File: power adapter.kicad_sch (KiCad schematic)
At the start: 12 parts

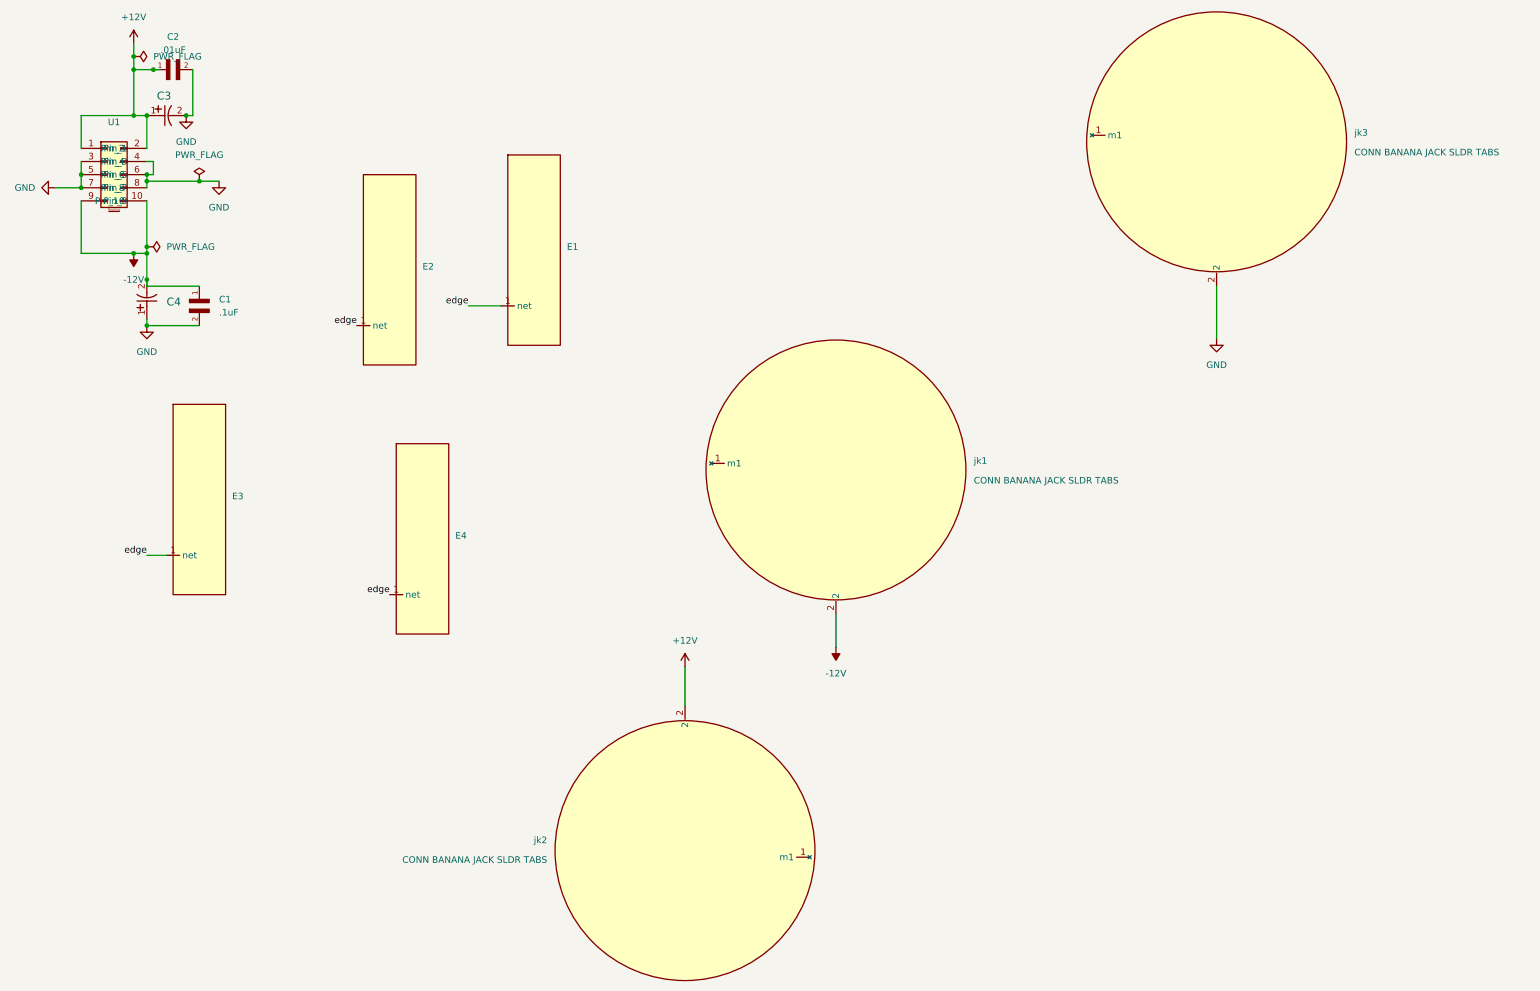
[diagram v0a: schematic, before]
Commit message: added default widths
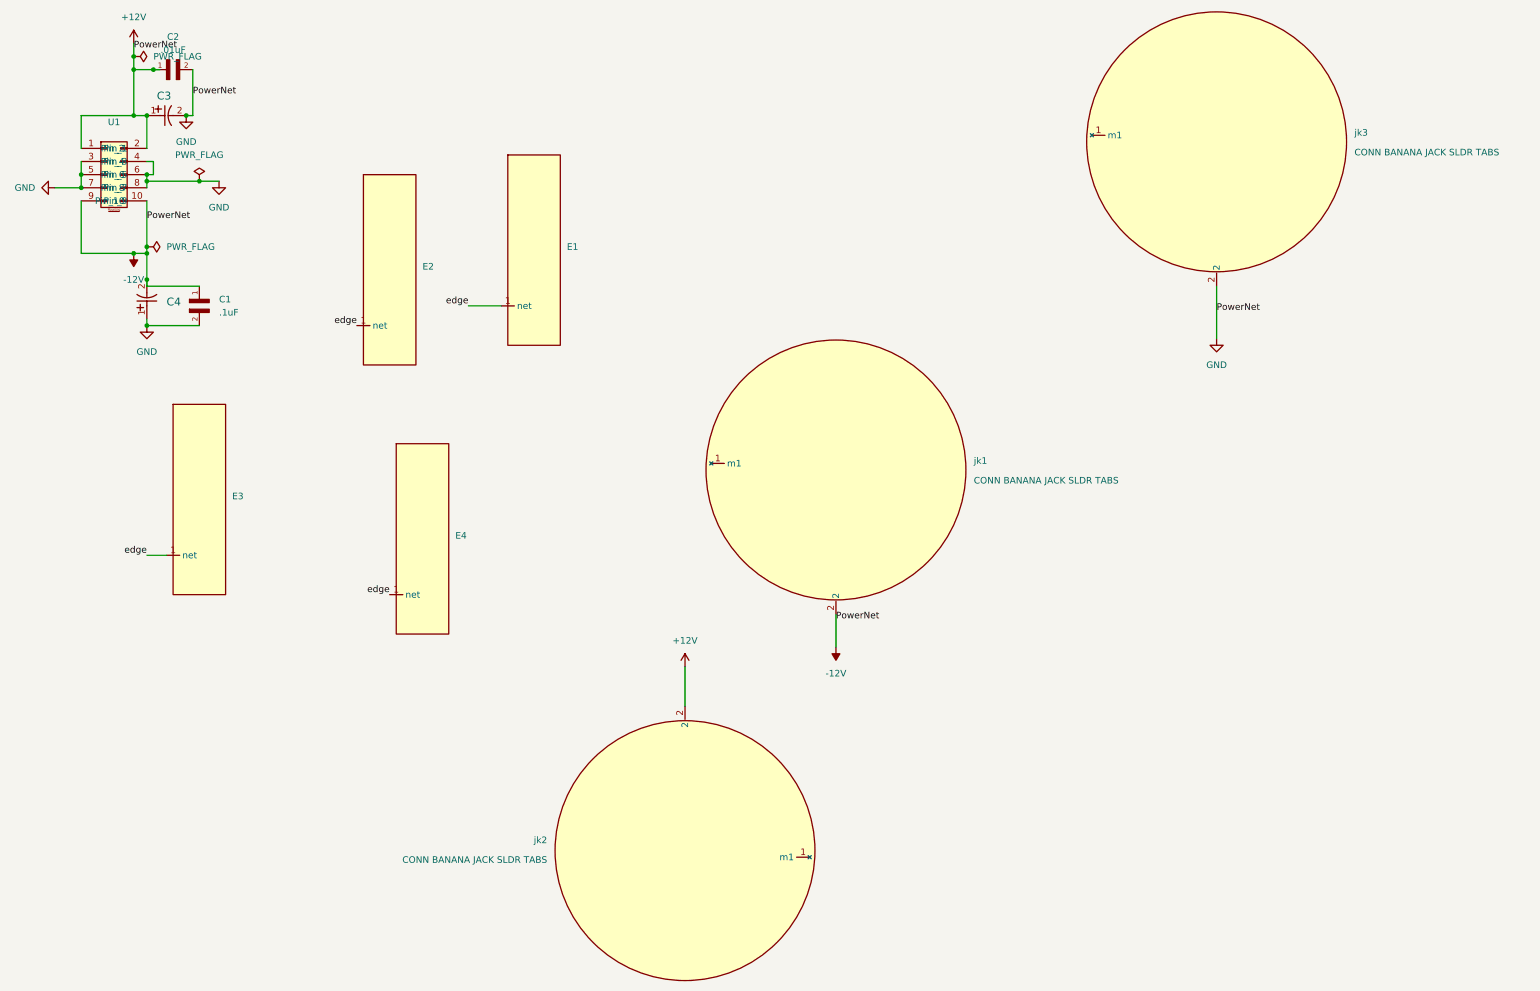
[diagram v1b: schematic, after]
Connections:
- net -12V is gone; now on net +12V: C1.1, C4.2, U1.10 (Pin_10), U1.9 (Pin_9), jk1.2
- net GND is gone; now on net +12V: C1.2, C2.2, C3.2, C4.1, U1.3 (Pin_3), U1.4 (Pin_4), U1.5 (Pin_5), U1.6 (Pin_6), U1.7 (Pin_7), U1.8 (Pin_8), jk3.2
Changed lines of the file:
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@@
+		)
+	)
+	(label "PowerNet"
+		(at 167.64 134.62 0)
+		(effects
+			(font
+				(size 1.27 1.27)
+			)
+			(justify left bottom)
+		)
+	)
+	(label "PowerNet"
+		(at 34.29 57.15 0)
+		(effects
+			(font
+				(size 1.27 1.27)
+			)
+			(justify left bottom)
+		)
+	)
+	(label "PowerNet"
+		(at 31.75 24.13 0)
+		(effects
+			(font
+				(size 1.27 1.27)
+			)
+			(justify left bottom)
 		)
 	)
@@
 			)
 			(justify right bottom)
+		)
+	)
+	(label "PowerNet"
+		(at 43.18 33.02 0)
+		(effects
+			(font
+				(size 1.27 1.27)
+			)
+			(justify left bottom)
 		)
 	)
@@
 		)
 	)
+	(label "PowerNet"
+		(at 241.3 74.93 0)
+		(effects
+			(font
+				(size 1.27 1.27)
+			)
+			(justify left bottom)
+		)
+	)

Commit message: Mk2firstCommit
more attention paid to fixing ERCs
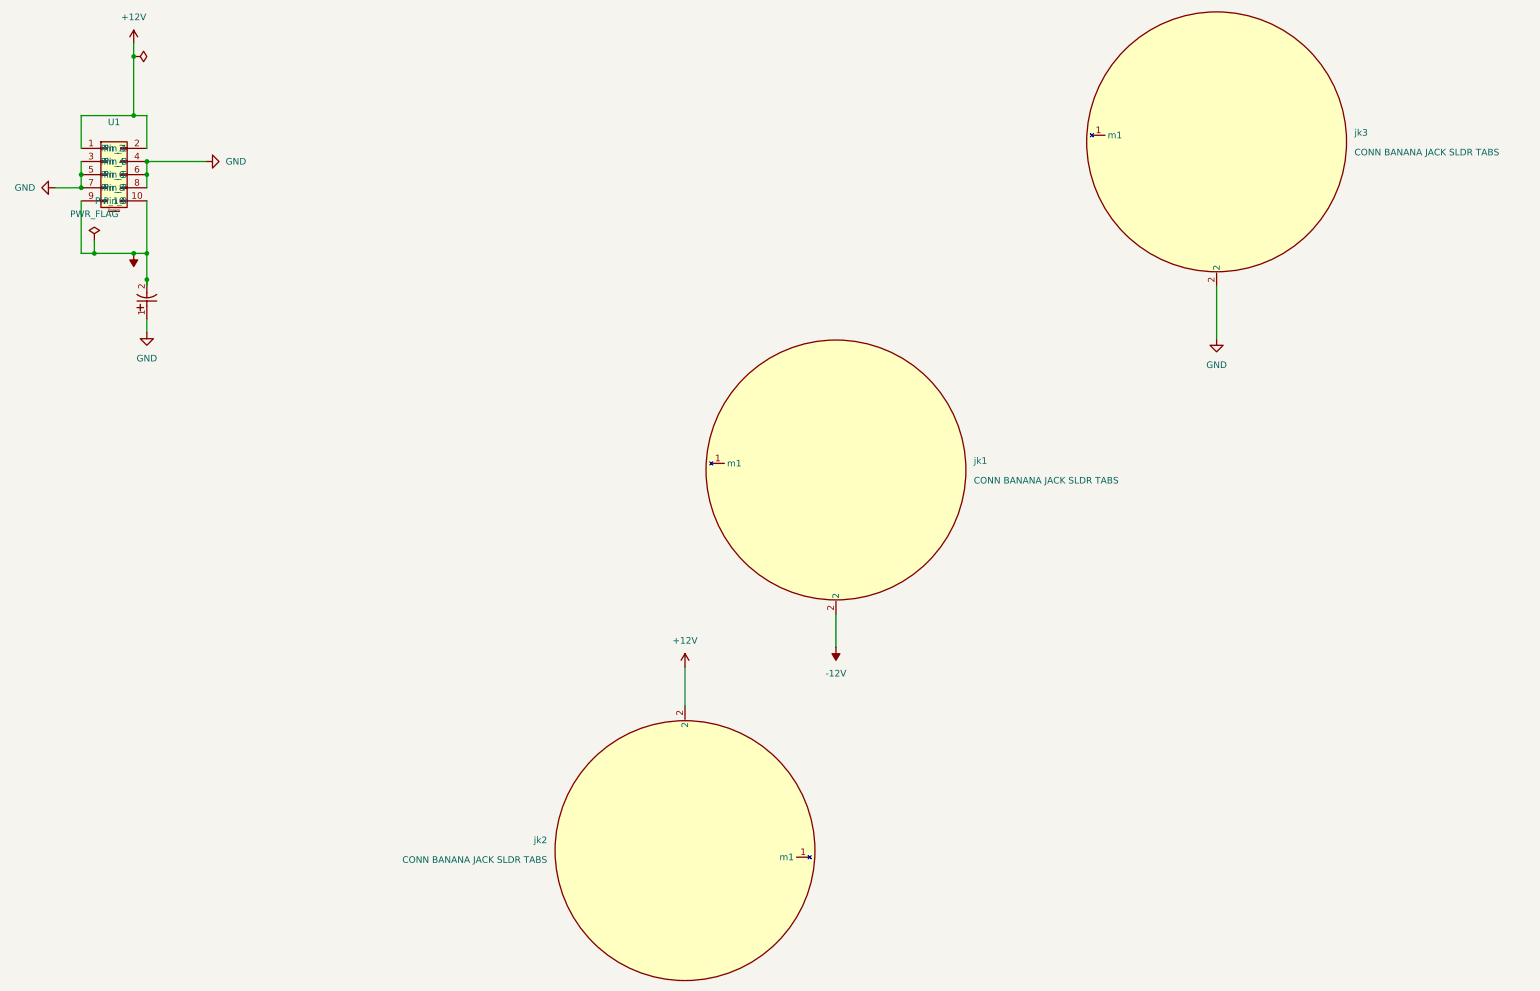
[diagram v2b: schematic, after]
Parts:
- removed C1: .1uF, adpterpcblib:CAPC1608X90N, symbol adapterlib:ceramiccap
- removed C2: .01uF, adpterpcblib:CAPC1608X90N, symbol adapterlib:ceramiccap
- removed C3: T491C106M025AT7280, customfootprints:10uFtantcap, symbol esp32lib:T491C106M025AT7280
- removed E1, E2, E3, E4: ~, adpterpcblib:edge, symbol adapterlib:Edge
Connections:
- net +12V: no longer C4.1, C4.2, U1.10 (Pin_10), U1.3 (Pin_3), U1.4 (Pin_4), U1.5 (Pin_5), U1.6 (Pin_6), U1.7 (Pin_7), U1.8 (Pin_8), U1.9 (Pin_9), jk1.2, jk3.2
- new net -12V: C4.2, U1.10 (Pin_10), U1.9 (Pin_9), jk1.2
- new net GND: C4.1, U1.3 (Pin_3), U1.4 (Pin_4), U1.5 (Pin_5), U1.6 (Pin_6), U1.7 (Pin_7), U1.8 (Pin_8), jk3.2
